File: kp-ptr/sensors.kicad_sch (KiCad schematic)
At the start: 26 parts

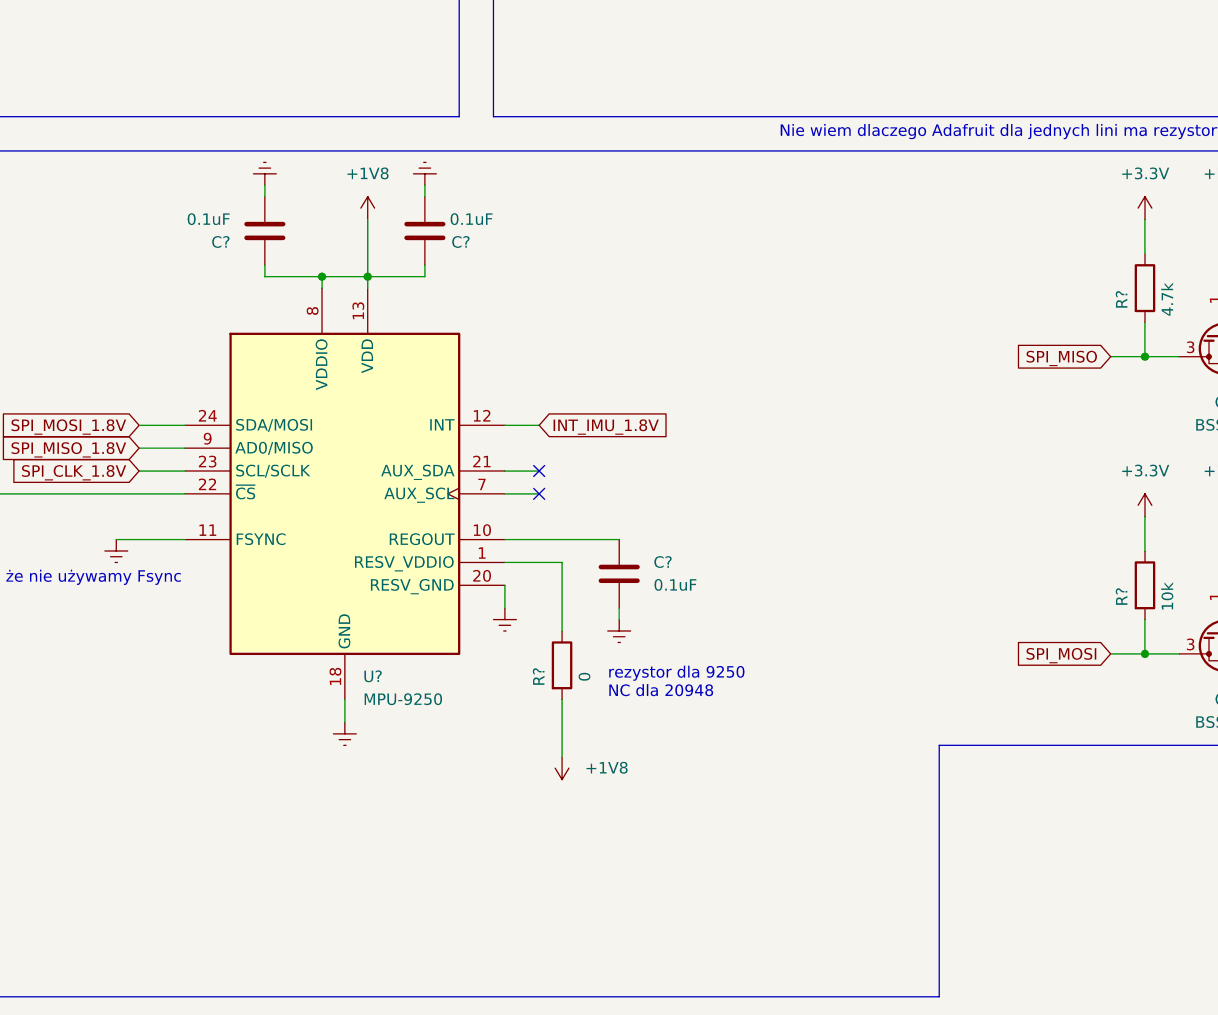
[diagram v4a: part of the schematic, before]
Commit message: IGN & PSU added
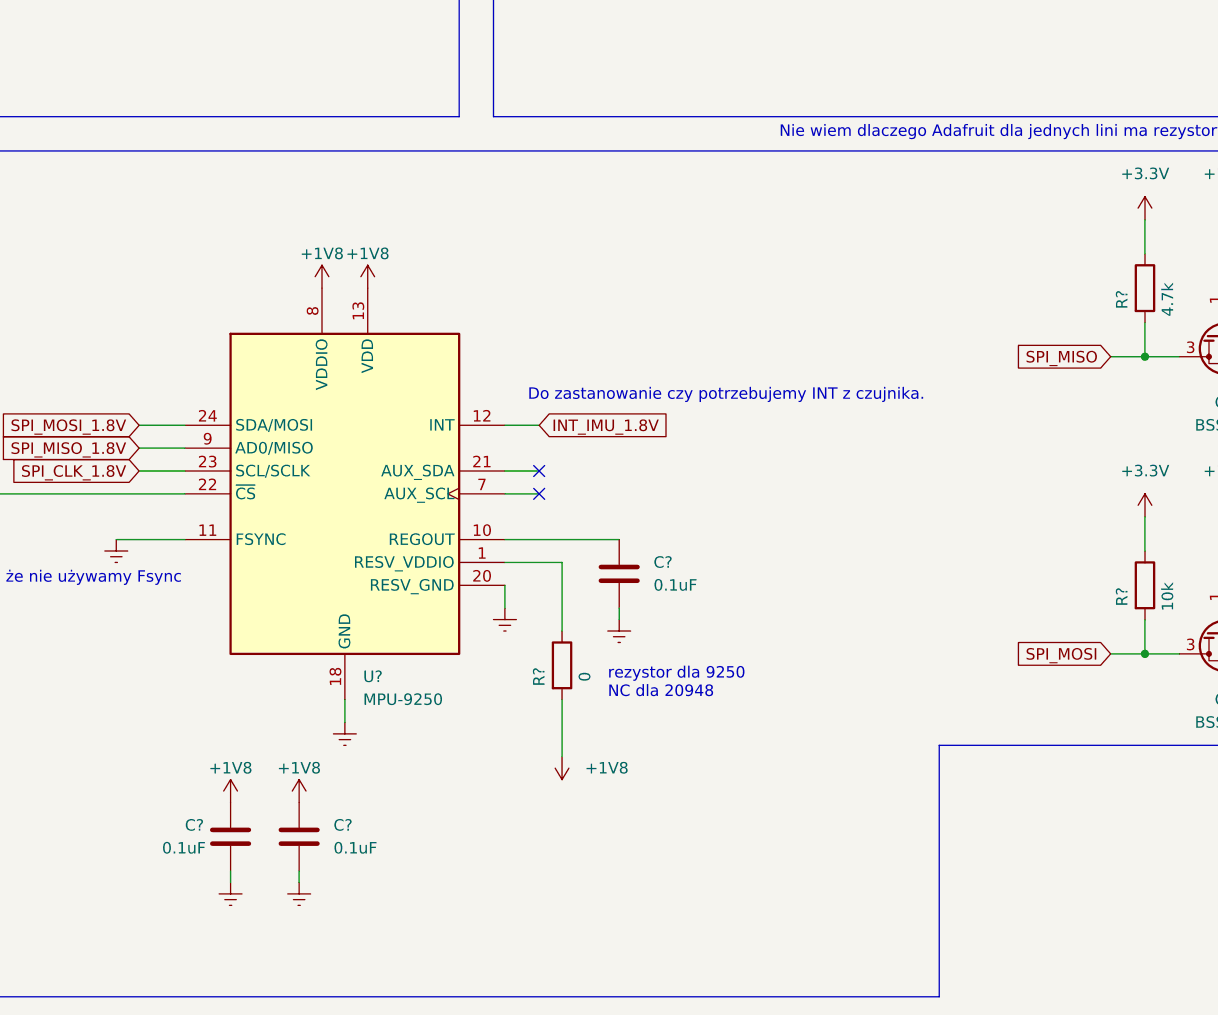
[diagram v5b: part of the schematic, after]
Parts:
- removed C? (x2): 0.1uF, symbol Device:C
- added C? (x2): 0.1uF, symbol Device:C
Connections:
- net +1V8: now also C?.1, C?.1
- net Earth: now also C?.2, C?.2
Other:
- note added: "Do zastanowanie czy potrzebujemy INT z czujnika."

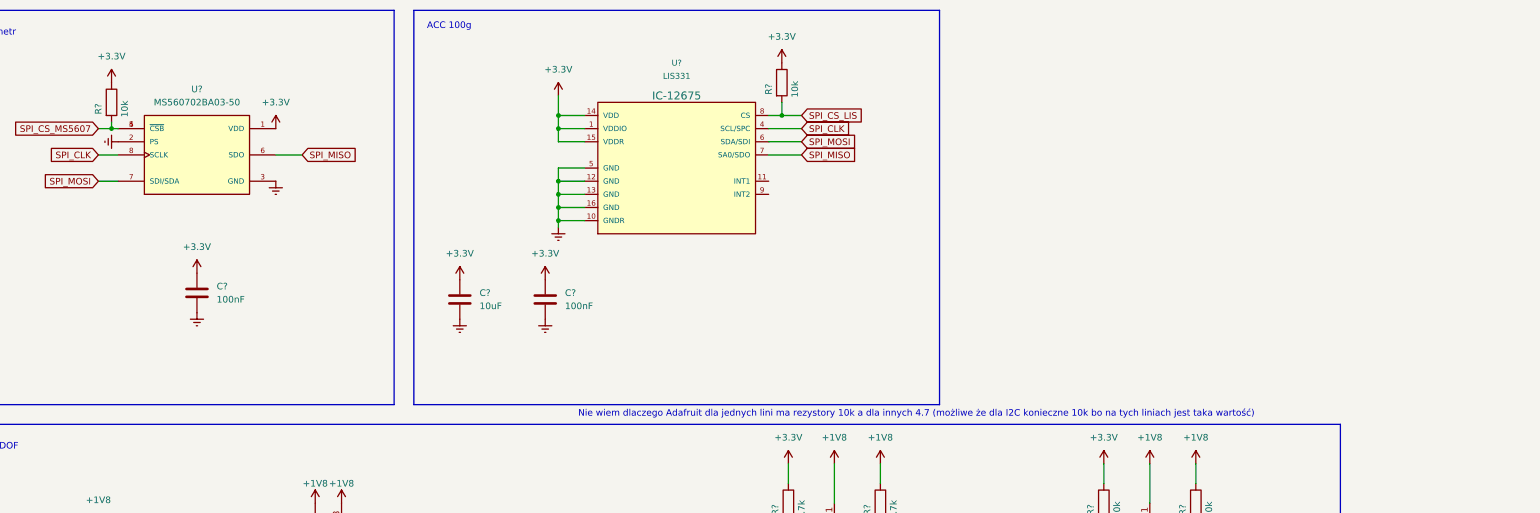
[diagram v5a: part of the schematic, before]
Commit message: LSM6DSO32 added
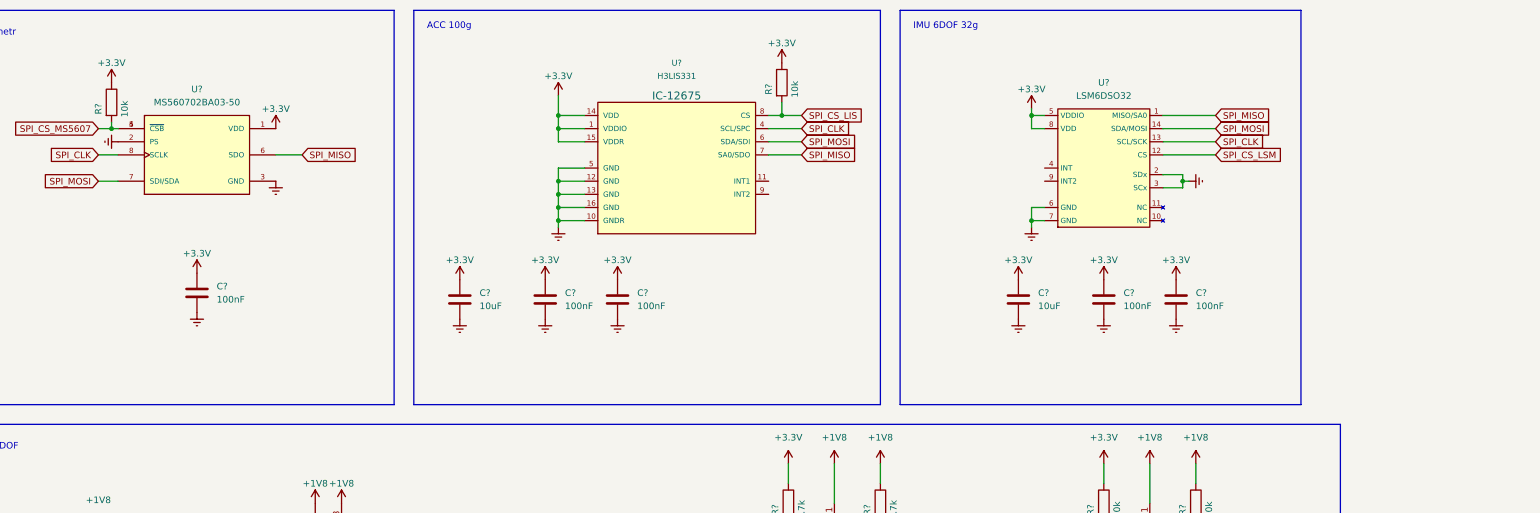
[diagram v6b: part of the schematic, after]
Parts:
- added C? (x3): 100nF, symbol Device:C
- added C?: 10uF, symbol Device:C
- added U?: LSM6DSO32, symbol KP-PTR_lib:LSM6DSO32
- U?: value LIS331 -> H3LIS331
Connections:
- net +3V3: now also C?.1, C?.1, C?.1, C?.1, U?.5 (VDDIO), U?.8 (VDD)
- net Earth: now also C?.2, C?.2, C?.2, C?.2, U?.2 (SDx), U?.3 (SCx), U?.6 (GND), U?.7 (GND)
- net SPI_CLK: now also U?.13 (SCL/SCK)
- net SPI_MISO: now also U?.1 (MISO/SA0)
- net SPI_MOSI: now also U?.14 (SDA/MOSI)
- new net SPI_CS_LSM: U?.12 (CS)
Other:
- note added: "IMU 6DOF 32g"
- note removed: "Nie wiem dlaczego Adafruit dla jednych lini ma rezystory 10k a dla innych 4.7 (możliwe że dla I2C konieczne 10k bo na tych liniach jest taka wartość)"

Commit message: Magnetometr Buzzer 3xLED Signed-off-by: kretu <krecik@gmail.com>
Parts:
- added C?: 1uF, symbol Device:C
- added C?: 10uF, symbol Device:C
- added U?: MMC5983MA, PQFN50P300X300X100-16N, symbol KP-PTR_lib:MMC5983MA
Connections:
- net +3V3: now also C?.1, U?.13 (VDDIO), U?.2 (VDD)
- net Earth: now also C?.2, C?.2, U?.11 (GND), U?.9 (GND)
- net SPI_CLK: now also U?.1 (SCL/SPI_SCK)
- net SPI_MISO: now also U?.5 (SPI_SDO)
- net SPI_MOSI: now also U?.16 (SDA/SPI_SDI)
- new net: C?.1, U?.10 (CAP)
- new net: U?.12 (NC), U?.14 (NC), U?.3 (NC), U?.6 (NC), U?.7 (NC), U?.8 (NC)
- new net SPI_CS_MAG: U?.4 (~{SPI_CS})
- no-connect marks 2 -> 7
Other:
- moved on the sheet: C?, D?, Q?, R?, U?

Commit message: GPS lora wrzucone symbole Signed-off-by: kretu <krecik@gmail.com>
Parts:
- added C?: 4.7uF, symbol Device:C
- added U?: CAM-M8Q-0, LCC100P960X1400X210-31N, symbol KP-PTR_lib:CAM-M8Q-0
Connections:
- net +3V3: now also C?.1, U?.1 (VCC_IO), U?.8 (V_BCKP), U?.9 (VCC)
- net Earth: now also C?.2, U?.10 (GND), U?.11 (GND), U?.12 (GND), U?.13 (GND), U?.14 (GND), U?.15 (GND), U?.18 (GND), U?.19 (GND), U?.21 (GND), U?.22 (GND), U?.27 (GND), U?.31 (GND), U?.4 (GND), U?.5 (GND)
- no-connect marks 7 -> 13
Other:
- note added: "GPS"
- note added: "Magnetometr"
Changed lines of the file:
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@@
   (junction (at -35.56 22.86) (diameter 0) (color 0 0 0 0)
   )
+  (junction (at 184.15 120.65) (diameter 0) (color 0 0 0 0)
+  )
   (junction (at 251.46 52.07) (diameter 0) (color 0 0 0 0)
   )
+  (junction (at 184.15 123.19) (diameter 0) (color 0 0 0 0)
+  )
   (junction (at 44.45 41.91) (diameter 0) (color 0 0 0 0)
   )
@@
   (junction (at 222.25 59.69) (diameter 0) (color 0 0 0 0)
   )
+  (no_connect (at 180.34 143.51))
+  (no_connect (at 180.34 146.05))
+  (no_connect (at 180.34 140.97))
+  (no_connect (at 180.34 135.89))
+  (no_connect (at 124.46 135.89))
+  (no_connect (at 124.46 138.43))
   (no_connect (at -181.61 38.1))
   (no_connect (at -181.61 35.56))
@@
     (stroke (width 0) (type default) (color 0 0 0 0))
   )
+  (wire (pts (xy 184.15 120.65) (xy 180.34 120.65))
+    (stroke (width 0) (type default) (color 0 0 0 0))
+  )
   (wire (pts (xy -203.2 63.5) (xy -203.2 60.96))
     (stroke (width 0) (type default) (color 0 0 0 0))
@@
     (stroke (width 0) (type default) (color 0 0 0 0))
   )
+  (wire (pts (xy 180.34 125.73) (xy 184.15 125.73))
+    (stroke (width 0) (type default) (color 0 0 0 0))
+  )
   (wire (pts (xy -53.34 22.86) (xy -49.53 22.86))
     (stroke (width 0) (type default) (color 0 0 0 0))
   )
+  (wire (pts (xy 185.42 151.13) (xy 180.34 151.13))
+    (stroke (width 0) (type default) (color 0 0 0 0))
+  )
   (wire (pts (xy -208.28 81.28) (xy -208.28 80.01))
     (stroke (width 0) (type default) (color 0 0 0 0))
@@
     (stroke (width 0) (type default) (color 0 0 0 0))
   )
+  (wire (pts (xy 184.15 125.73) (xy 184.15 123.19))
+    (stroke (width 0) (type default) (color 0 0 0 0))
+  )
   (wire (pts (xy -53.34 55.88) (xy -49.53 55.88))
     (stroke (width 0) (type default) (color 0 0 0 0))
@@
     (stroke (width 0) (type default) (color 0 0 0 0))
   )
+  (wire (pts (xy 143.51 170.18) (xy 143.51 173.99))
+    (stroke (width 0) (type default) (color 0 0 0 0))
+  )
   (wire (pts (xy 135.89 49.53) (xy 130.81 49.53))
     (stroke (width 0) (type default) (color 0 0 0 0))
@@
     (stroke (width 0) (type default) (color 0 0 0 0))
   )
+  (wire (pts (xy 143.51 181.61) (xy 143.51 184.15))
+    (stroke (width 0) (type default) (color 0 0 0 0))
+  )
   (wire (pts (xy -100.33 55.88) (xy -96.52 55.88))
     (stroke (width 0) (type default) (color 0 0 0 0))
@@
     (stroke (width 0) (type default) (color 0 0 0 0))
   )
+  (wire (pts (xy 184.15 123.19) (xy 184.15 120.65))
+    (stroke (width 0) (type default) (color 0 0 0 0))
+  )
   (wire (pts (xy -181.61 30.48) (xy -185.42 30.48))
     (stroke (width 0) (type default) (color 0 0 0 0))
@@
   )
   (wire (pts (xy -185.42 45.72) (xy -179.07 45.72))
+    (stroke (width 0) (type default) (color 0 0 0 0))
+  )
+  (wire (pts (xy 180.34 123.19) (xy 184.15 123.19))
     (stroke (width 0) (type default) (color 0 0 0 0))
   )
@@
     (effects (font (size 1.27 1.27)) (justify left bottom))
   )
+  (text "Magnetometr" (at 22.86 115.57 0)
+    (effects (font (size 1.27 1.27)) (justify left bottom))
+  )
   (text "rezystor dla 9250\nNC dla 20948" (at -173.99 60.96 0)
     (effects (font (size 1.27 1.27)) (justify left bottom))
   )
   (text "IMU 6DOF 32g" (at 199.39 22.86 0)
+    (effects (font (size 1.27 1.27)) (justify left bottom))
+  )
+  (text "GPS" (at 105.41 115.57 0)
     (effects (font (size 1.27 1.27)) (justify left bottom))
   )
@@
     )
     (property "Datasheet" "" (id 3) (at -35.56 7.62 0)
+      (effects (font (size 1.27 1.27)) hide)
+    )
+    (pin "1")
+  )
+  (symbol (lib_id "Device:C") (at 143.51 177.8 0) (unit 1)
+    (in_bom yes) (on_board yes) (fields_autoplaced)
+    (property "Reference" "C?" (id 0) (at 147.32 176.5299 0)
+      (effects (font (size 1.27 1.27)) (justify left))
+    )
+    (property "Value" "4.7uF" (id 1) (at 147.32 179.0699 0)
+      (effects (font (size 1.27 1.27)) (justify left))
+    )
+    (property "Footprint" "" (id 2) (at 144.4752 181.61 0)
+      (effects (font (size 1.27 1.27)) hide)
+    )
+    (property "Datasheet" "~" (id 3) (at 143.51 177.8 0)
+      (effects (font (size 1.27 1.27)) hide)
+    )
+    (pin "1")
+    (pin "2")
+  )
+  (symbol (lib_id "power:+3.3V") (at 143.51 170.18 0) (unit 1)
+    (in_bom yes) (on_board yes)
+    (property "Reference" "#PWR?" (id 0) (at 143.51 173.99 0)
+      (effects (font (size 1.27 1.27)) hide)
+    )
+    (property "Value" "+3.3V" (id 1) (at 143.51 166.37 0))
+    (property "Footprint" "" (id 2) (at 143.51 170.18 0)
+      (effects (font (size 1.27 1.27)) hide)
+    )
+    (property "Datasheet" "" (id 3) (at 143.51 170.18 0)
       (effects (font (size 1.27 1.27)) hide)
     )
@@
     (pin "1")
   )
+  (symbol (lib_id "power:+3.3V") (at 184.15 120.65 0) (unit 1)
+    (in_bom yes) (on_board yes)
+    (property "Reference" "#PWR?" (id 0) (at 184.15 124.46 0)
+      (effects (font (size 1.27 1.27)) hide)
+    )
+    (property "Value" "+3.3V" (id 1) (at 184.15 116.84 0))
+    (property "Footprint" "" (id 2) (at 184.15 120.65 0)
+      (effects (font (size 1.27 1.27)) hide)
+    )
+    (property "Datasheet" "" (id 3) (at 184.15 120.65 0)
+      (effects (font (size 1.27 1.27)) hide)
+    )
+    (pin "1")
+  )
   (symbol (lib_id "Device:R") (at 173.99 33.02 0) (unit 1)
     (in_bom yes) (on_board yes)
@@
     (pin "1")
   )
+  (symbol (lib_id "power:Earth") (at 143.51 184.15 0) (unit 1)
+    (in_bom yes) (on_board yes) (fields_autoplaced)
+    (property "Reference" "#PWR?" (id 0) (at 143.51 190.5 0)
+      (effects (font (size 1.27 1.27)) hide)
+    )
+    (property "Value" "Earth" (id 1) (at 143.51 187.96 0)
+      (effects (font (size 1.27 1.27)) hide)
+    )
+    (property "Footprint" "" (id 2) (at 143.51 184.15 0)
+      (effects (font (size 1.27 1.27)) hide)
+    )
+    (property "Datasheet" "~" (id 3) (at 143.51 184.15 0)
+      (effects (font (size 1.27 1.27)) hide)
+    )
+    (pin "1")
+  )
+  (symbol (lib_id "KP-PTR_lib:CAM-M8Q-0") (at 152.4 135.89 0) (unit 1)
+    (in_bom yes) (on_board yes) (fields_autoplaced)
+    (property "Reference" "U?" (id 0) (at 152.4 113.03 0))
+    (property "Value" "CAM-M8Q-0" (id 1) (at 152.4 115.57 0))
+    (property "Footprint" "LCC100P960X1400X210-31N" (id 2) (at 152.4 135.89 0)
+      (effects (font (size 1.27 1.27)) (justify left bottom) hide)
+    )
+    (property "Datasheet" "" (id 3) (at 152.4 135.89 0)
+      (effects (font (size 1.27 1.27)) (justify left bottom) hide)
+    )
+    (property "MANUFACTURER" "UBlox" (id 4) (at 152.4 135.89 0)
+      (effects (font (size 1.27 1.27)) (justify left bottom) hide)
+    )
+    (pin "1")
+    (pin "10")
+    (pin "11")
+    (pin "12")
+    (pin "13")
+    (pin "14")
+    (pin "15")
+    (pin "16")
+    (pin "17")
+    (pin "18")
+    (pin "19")
+    (pin "2")
+    (pin "20")
+    (pin "21")
+    (pin "22")
+    (pin "23")
+    (pin "24")
+    (pin "25")
+    (pin "26")
+    (pin "27")
+    (pin "28")
+    (pin "29")
+    (pin "3")
+    (pin "30")
+    (pin "31")
+    (pin "4")
+    (pin "5")
+    (pin "6")
+    (pin "7")
+    (pin "8")
+    (pin "9")
+  )
   (symbol (lib_id "power:Earth") (at 128.27 78.74 0) (unit 1)
     (in_bom yes) (on_board yes) (fields_autoplaced)
@@
       (effects (font (size 1.27 1.27)) hide)
     )
+    (pin "1")
+  )
+  (symbol (lib_id "power:Earth") (at 185.42 151.13 0) (unit 1)
+    (in_bom yes) (on_board yes) (fields_autoplaced)
+    (property "Reference" "#PWR?" (id 0) (at 185.42 157.48 0)
+      (effects (font (size 1.27 1.27)) hide)
+    )
+    (property "Value" "Earth" (id 1) (at 185.42 154.94 0)
+      (effects (font (size 1.27 1.27)) hide)
+    )
+    (property "Footprint" "" (id 2) (at 185.42 151.13 0)
+      (effects (font (size 1.27 1.27)) hide)
+    )
+    (property "Datasheet" "~" (id 3) (at 185.42 151.13 0)
+      (effects (font (size 1.27 1.27)) hide)
+    )
